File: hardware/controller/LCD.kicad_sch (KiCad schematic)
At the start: 1 part, among them U1 3.2inch_IPS_SPI_Module_ILI9341

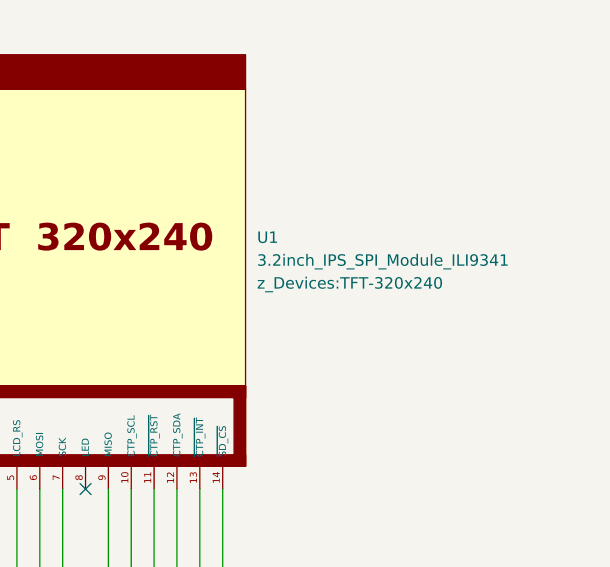
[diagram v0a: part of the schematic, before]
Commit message: finished first rev of controller schematic minus actually finding passive components. moved some features to rev2 todo
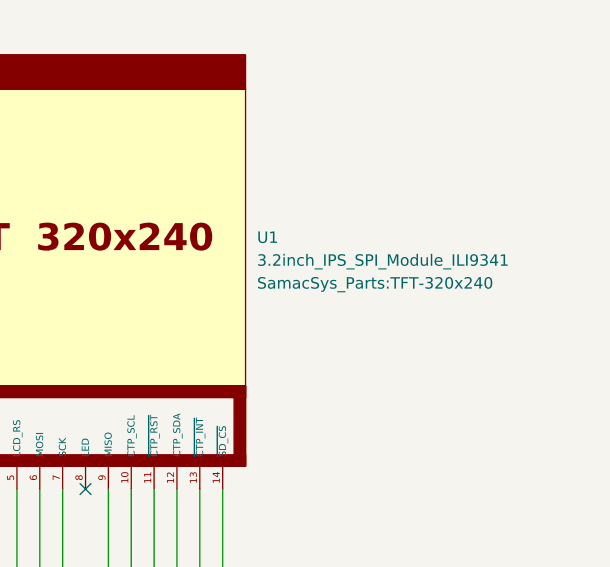
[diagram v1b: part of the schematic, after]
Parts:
- U1: footprint z_Devices:TFT-320x240 -> SamacSys_Parts:TFT-320x240
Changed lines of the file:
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@@
 	)
 	(bus_alias "SPI_LCD_SD"
-		(members "LCD_RST" "SCK" "MOSI" "SD_CS" "MISO" "LCD_CS")
+		(members "LCD_RST" "SCK" "MOSI" "SD_CS" "MISO" "LCD_CS" "LCD_RS")
 	)
 	(no_connect
@@
 			)
 		)
-		(property "Footprint" "z_Devices:TFT-320x240"
+		(property "Footprint" "SamacSys_Parts:TFT-320x240"
 			(at 157.48 74.9299 0)
 			(effects

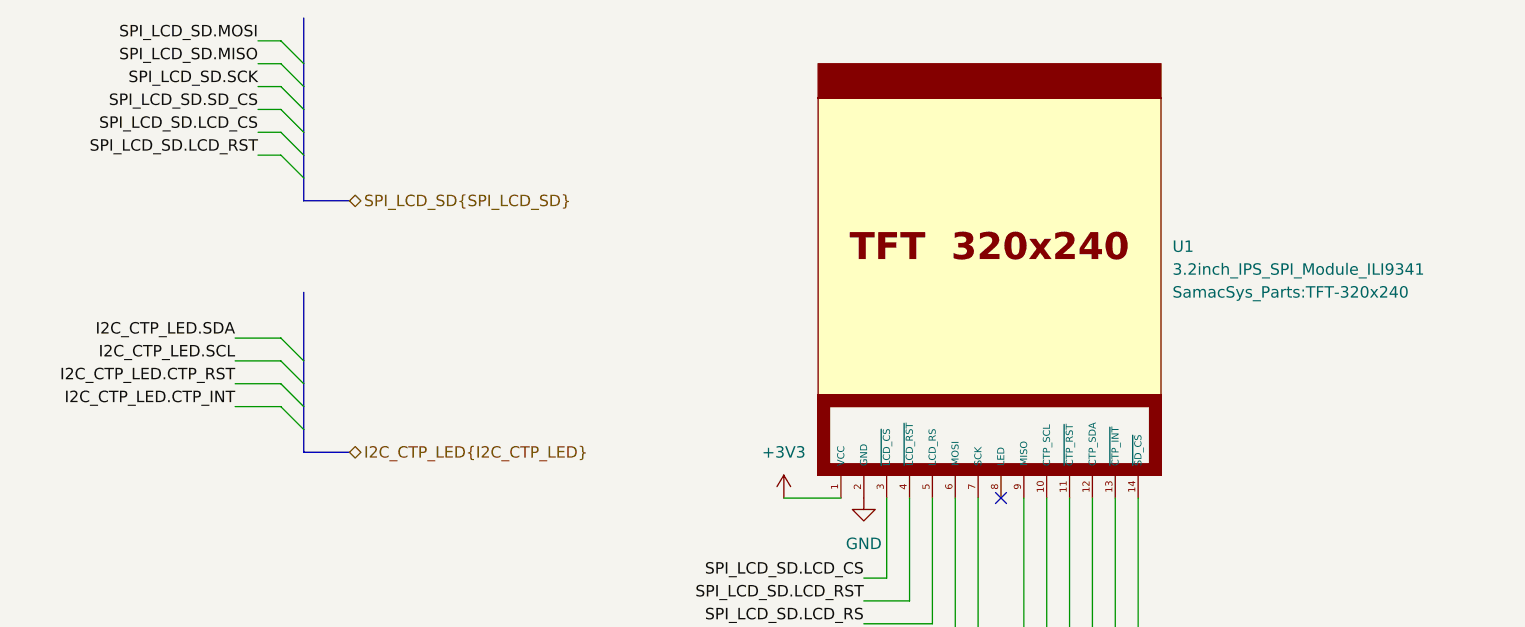
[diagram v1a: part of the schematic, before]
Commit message: Moved LEDs around. Replaced some discrete resistors with resistor arrays. Added mounting holes. Added. Added a lot of actual components for passive elements
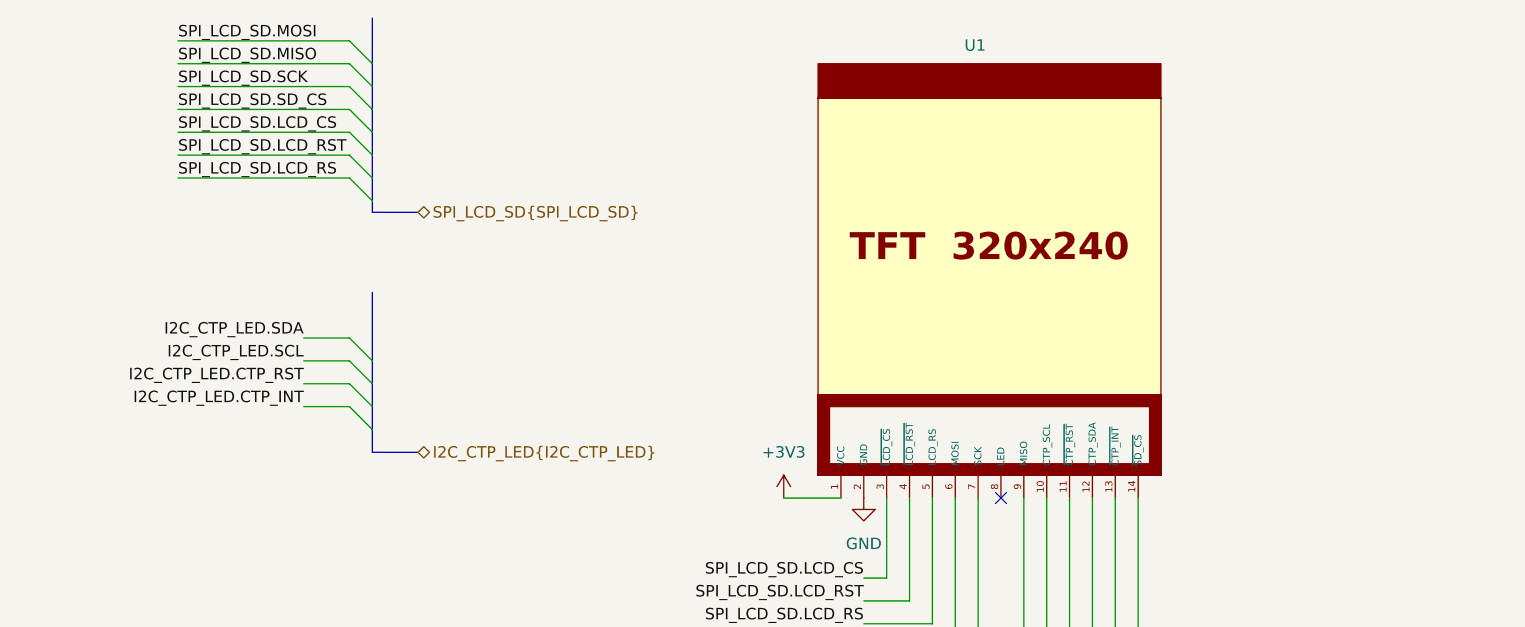
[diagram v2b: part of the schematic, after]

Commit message: ERC good to go. grouped all components on pcb
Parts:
- renumbered U1 to U501
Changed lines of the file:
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@@
 		(dnp no)
 		(fields_autoplaced yes)
-		(property "Reference" "#PWR038"
+		(property "Reference" "#PWR0502"
 			(at 123.19 104.14 0)
 			(effects
@@
 			(project ""
 				(path "/869bea87-c885-4ead-826b-3f34ceacafad/a91903fe-ee0b-42c2-9d54-da8a7ff8ed7e"
-					(reference "#PWR038")
+					(reference "#PWR0502")
 					(unit 1)
 				)
@@
 		(dnp no)
 		(fields_autoplaced yes)
-		(property "Reference" "#PWR037"
+		(property "Reference" "#PWR0501"
 			(at 114.3 101.6 0)
 			(effects
@@
 			(project ""
 				(path "/869bea87-c885-4ead-826b-3f34ceacafad/a91903fe-ee0b-42c2-9d54-da8a7ff8ed7e"
-					(reference "#PWR037")
+					(reference "#PWR0501")
 					(unit 1)
 				)
@@
 		(on_board yes)
 		(dnp no)
-		(property "Reference" "U1"
+		(property "Reference" "U501"
 			(at 134.366 47.498 0)
 			(effects
@@
 			(project ""
 				(path "/869bea87-c885-4ead-826b-3f34ceacafad/a91903fe-ee0b-42c2-9d54-da8a7ff8ed7e"
-					(reference "U1")
+					(reference "U501")
 					(unit 1)
 				)

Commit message: man im tired
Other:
- note added: "todo: check if i need to downgrade thew size of this chonker"
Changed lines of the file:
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@@
 		(members "LCD_RST" "SCK" "MOSI" "SD_CS" "MISO" "LCD_CS" "LCD_RS")
+	)
+	(text "todo: check if i need to downgrade thew size of this chonker"
+		(exclude_from_sim no)
+		(at 141.224 39.37 0)
+		(effects
+			(font
+				(size 1.27 1.27)
+			)
+		)
 	)
 	(no_connect

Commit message: save before nuke
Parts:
- renumbered U501 to U101
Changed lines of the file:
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@@
 		(dnp no)
 		(fields_autoplaced yes)
-		(property "Reference" "#PWR0502"
+		(property "Reference" "#PWR0139"
 			(at 123.19 104.14 0)
 			(effects
@@
 			(project ""
 				(path "/869bea87-c885-4ead-826b-3f34ceacafad/a91903fe-ee0b-42c2-9d54-da8a7ff8ed7e"
-					(reference "#PWR0502")
+					(reference "#PWR0139")
 					(unit 1)
 				)
@@
 		(dnp no)
 		(fields_autoplaced yes)
-		(property "Reference" "#PWR0501"
+		(property "Reference" "#PWR0138"
 			(at 114.3 101.6 0)
 			(effects
@@
 			(project ""
 				(path "/869bea87-c885-4ead-826b-3f34ceacafad/a91903fe-ee0b-42c2-9d54-da8a7ff8ed7e"
-					(reference "#PWR0501")
+					(reference "#PWR0138")
 					(unit 1)
 				)
@@
 		(on_board yes)
 		(dnp no)
-		(property "Reference" "U501"
+		(property "Reference" "U101"
 			(at 134.366 47.498 0)
 			(effects
@@
 			(project ""
 				(path "/869bea87-c885-4ead-826b-3f34ceacafad/a91903fe-ee0b-42c2-9d54-da8a7ff8ed7e"
-					(reference "U501")
+					(reference "U101")
 					(unit 1)
 				)

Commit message: forgor
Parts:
- added U2: 3.2inch_IPS_SPI_Module_ILI9341, SamacSys_Parts:TFT-320x240, symbol SamacSys_Parts:2.4inch_IPS_SPI_Module_ILI9341
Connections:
- net +3V3: now also U2.1 (VCC)
- net GND: now also U2.2 (GND)
- net SPI_LCD_SD.LCD_CS: now also U2.3 (~{LCD_CS})
- net SPI_LCD_SD.LCD_RS: now also U2.5 (LCD_RS)
- net SPI_LCD_SD.LCD_RST: now also U2.4 (~{LCD_RST})
- net SPI_LCD_SD.MISO: now also U2.13 (T_DO), U2.9 (MISO)
- net SPI_LCD_SD.MOSI: now also U2.12 (T_DIN), U2.6 (MOSI)
- net SPI_LCD_SD.SCK: now also U2.10 (T_CLK), U2.7 (SCK)
- new net SPI_LCD_SD.TCH_CS: U2.11 (T_CS)
- new net SPI_LCD_SD.TCH_IRQ: U2.14 (T_IRQ)
- no-connect marks 1 -> 2
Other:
- note added: "Capacitive Touchscreen LCD"
- note added: "Hierarchical Pins"
- note added: "Note: I2C pullups handled in LED schematic"
- note added: "Resistive Touchscreen LCD"
- note added: "YES there are two LCDs, but only one can be installed at a time. I did this because I wanted flexibility for what kind of screen I could use Capacitive one uses SPI for display + I2C for touchscreen Resistive one uses SPI for both"
- note removed: "todo: check if i need to downgrade thew size of this chonker"
- moved on the sheet: U101

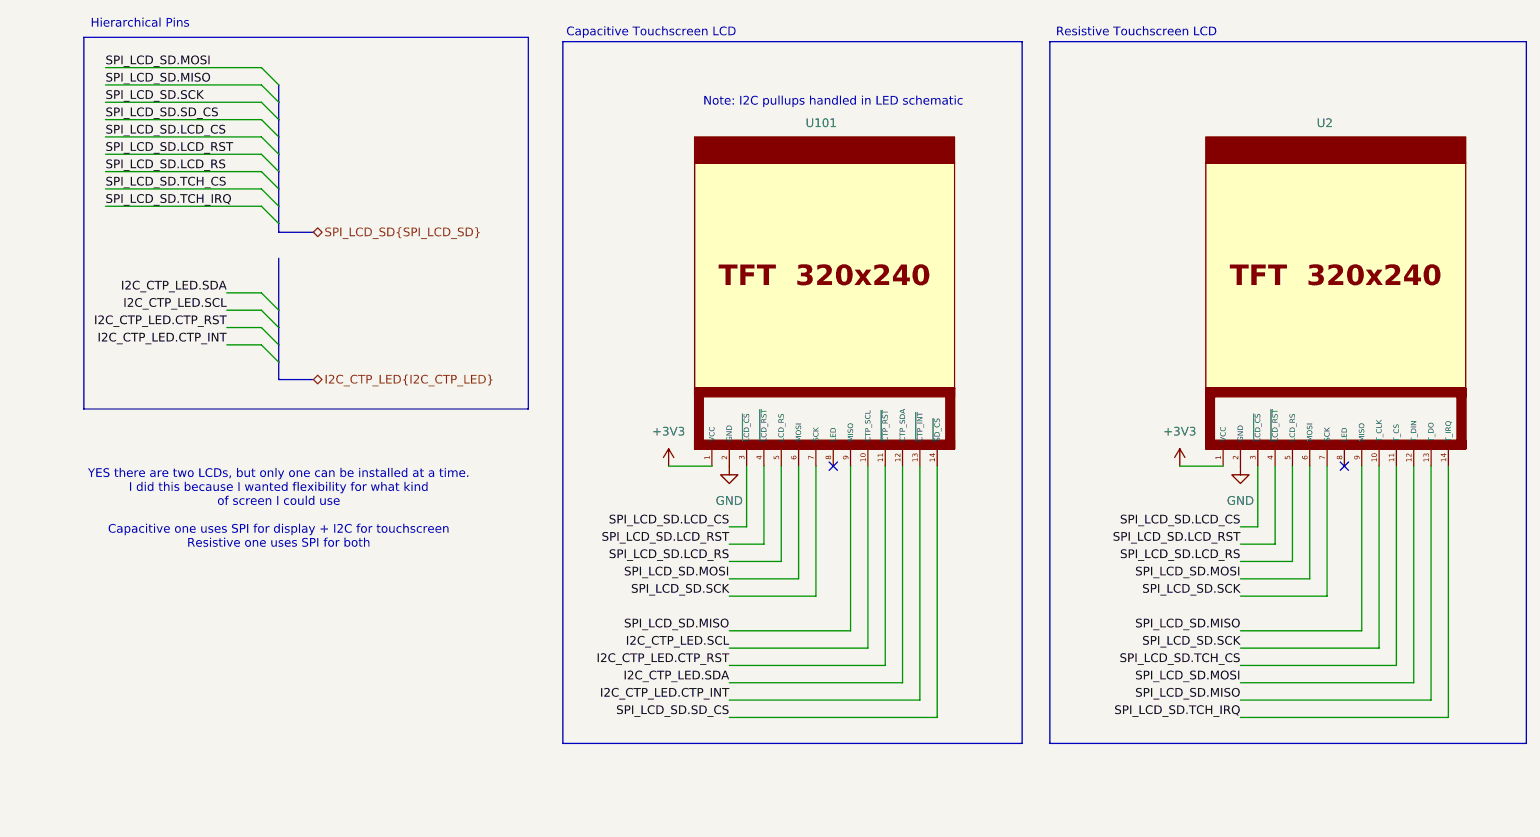
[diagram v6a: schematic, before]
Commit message: clean up DRC. need to add stitching vias and figure out why inner ground plane isnt connected to F.Cu pour
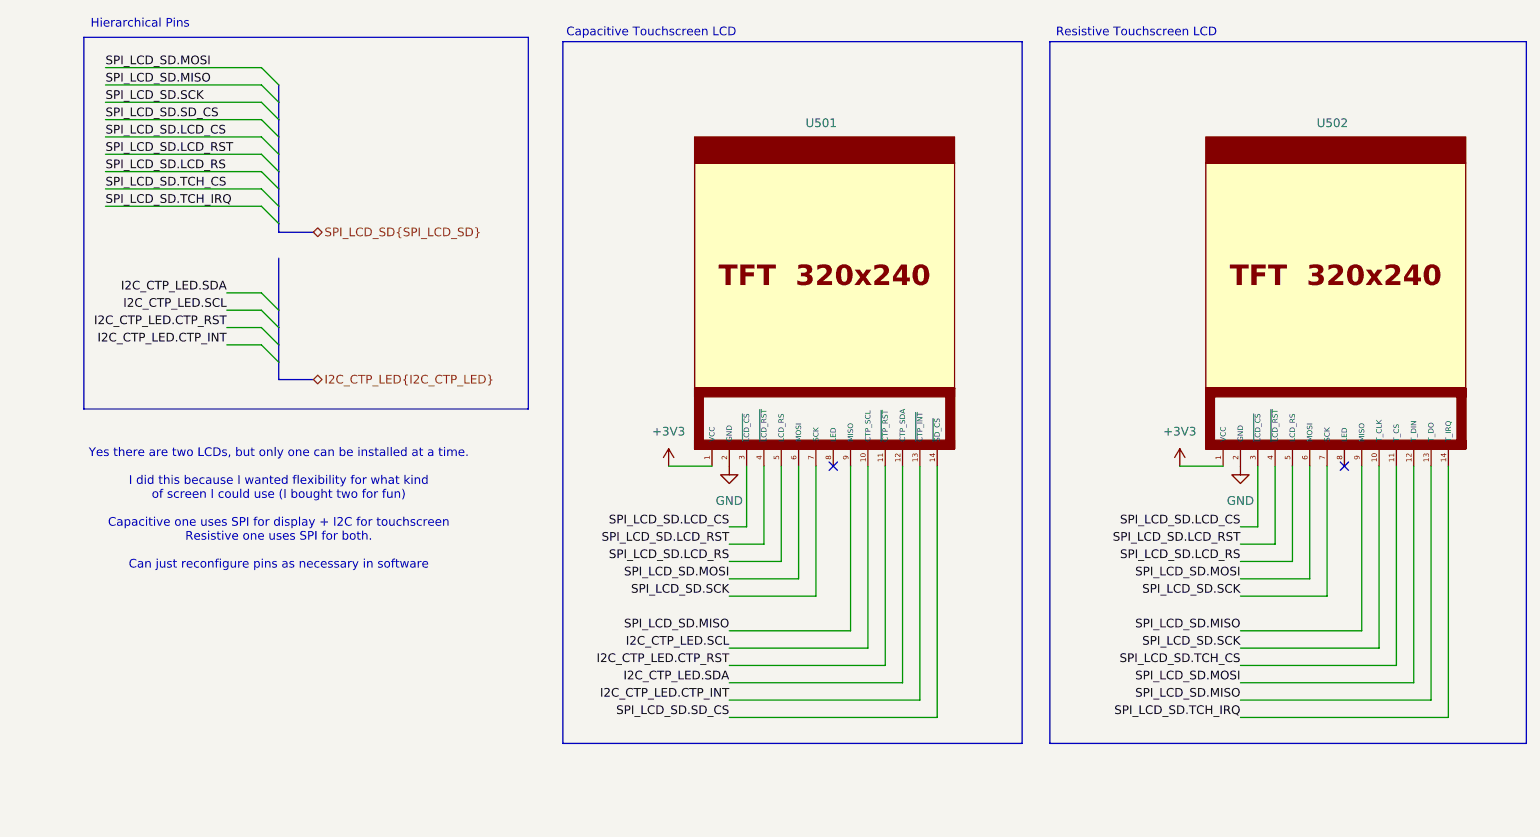
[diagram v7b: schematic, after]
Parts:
- renumbered U101 to U501, U2 to U502
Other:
- note added: "Yes there are two LCDs, but only one can be installed at a time. I did this because I wanted flexibility for what kind of screen I could use (I bought two for fun) Capacitive one uses SPI for display + I2C for touchscreen Resistive one uses SPI for both. Can just reconfigure pins as necessary in software"
- note removed: "Note: I2C pullups handled in LED schematic"
- note removed: "YES there are two LCDs, but only one can be installed at a time. I did this because I wanted flexibility for what kind of screen I could use Capacitive one uses SPI for display + I2C for touchscreen Resistive one uses SPI for both"
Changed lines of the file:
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@@
 		)
 	)
-	(text "YES there are two LCDs, but only one can be installed at a time.\nI did this because I wanted flexibility for what kind\nof screen I could use\n\nCapacitive one uses SPI for display + I2C for touchscreen\nResistive one uses SPI for both"
+	(text "Yes there are two LCDs, but only one can be installed at a time.\n\nI did this because I wanted flexibility for what kind\nof screen I could use (I bought two for fun)\n\nCapacitive one uses SPI for display + I2C for touchscreen\nResistive one uses SPI for both.\n\nCan just reconfigure pins as necessary in software"
 		(exclude_from_sim no)
 		(at 54.61 88.9 0)
@@
 		(exclude_from_sim no)
 		(at 180.34 19.05 0)
-		(effects
-			(font
-				(size 1.27 1.27)
-			)
-		)
-	)
-	(text "Note: I2C pullups handled in LED schematic"
-		(exclude_from_sim no)
-		(at 135.89 29.21 0)
 		(effects
 			(font
@@
 		(dnp no)
 		(fields_autoplaced yes)
-		(property "Reference" "#PWR0139"
+		(property "Reference" "#PWR0502"
 			(at 120.65 88.9 0)
 			(effects
@@
 			(project ""
 				(path "/869bea87-c885-4ead-826b-3f34ceacafad/a91903fe-ee0b-42c2-9d54-da8a7ff8ed7e"
-					(reference "#PWR0139")
+					(reference "#PWR0502")
 					(unit 1)
 				)
@@
 		(dnp no)
 		(fields_autoplaced yes)
-		(property "Reference" "#PWR0138"
+		(property "Reference" "#PWR0501"
 			(at 111.76 86.36 0)
 			(effects
@@
 			(project ""
 				(path "/869bea87-c885-4ead-826b-3f34ceacafad/a91903fe-ee0b-42c2-9d54-da8a7ff8ed7e"
-					(reference "#PWR0138")
+					(reference "#PWR0501")
 					(unit 1)
 				)
@@
 		(dnp no)
 		(fields_autoplaced yes)
-		(property "Reference" "#PWR018"
+		(property "Reference" "#PWR0503"
 			(at 186.69 86.36 0)
 			(effects
@@
 			(project "controller"
 				(path "/869bea87-c885-4ead-826b-3f34ceacafad/a91903fe-ee0b-42c2-9d54-da8a7ff8ed7e"
-					(reference "#PWR018")
+					(reference "#PWR0503")
 					(unit 1)
 				)
@@
 		(on_board yes)
 		(dnp no)
-		(property "Reference" "U2"
+		(property "Reference" "U502"
 			(at 206.756 32.258 0)
 			(effects
@@
 			(project "controller"
 				(path "/869bea87-c885-4ead-826b-3f34ceacafad/a91903fe-ee0b-42c2-9d54-da8a7ff8ed7e"
-					(reference "U2")
+					(reference "U502")
 					(unit 1)
 				)
@@
 		(on_board yes)
 		(dnp no)
-		(property "Reference" "U101"
+		(property "Reference" "U501"
 			(at 131.826 32.258 0)
 			(effects
@@
 			(project ""
 				(path "/869bea87-c885-4ead-826b-3f34ceacafad/a91903fe-ee0b-42c2-9d54-da8a7ff8ed7e"
-					(reference "U101")
+					(reference "U501")
 					(unit 1)
 				)
@@
 		(dnp no)
 		(fields_autoplaced yes)
-		(property "Reference" "#PWR019"
+		(property "Reference" "#PWR0504"
 			(at 195.58 88.9 0)
 			(effects
@@
 			(project "controller"
 				(path "/869bea87-c885-4ead-826b-3f34ceacafad/a91903fe-ee0b-42c2-9d54-da8a7ff8ed7e"
-					(reference "#PWR019")
+					(reference "#PWR0504")
 					(unit 1)
 				)
